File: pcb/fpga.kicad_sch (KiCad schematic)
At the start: 60 parts, among them J1 DE15_Socket_HighDensity, U1 XC7A50T-FTG256, U2 410-251-B, U3 S70KL1283DPBHV020, U4 W25Q128JVS, Y1 ASE-20MHz

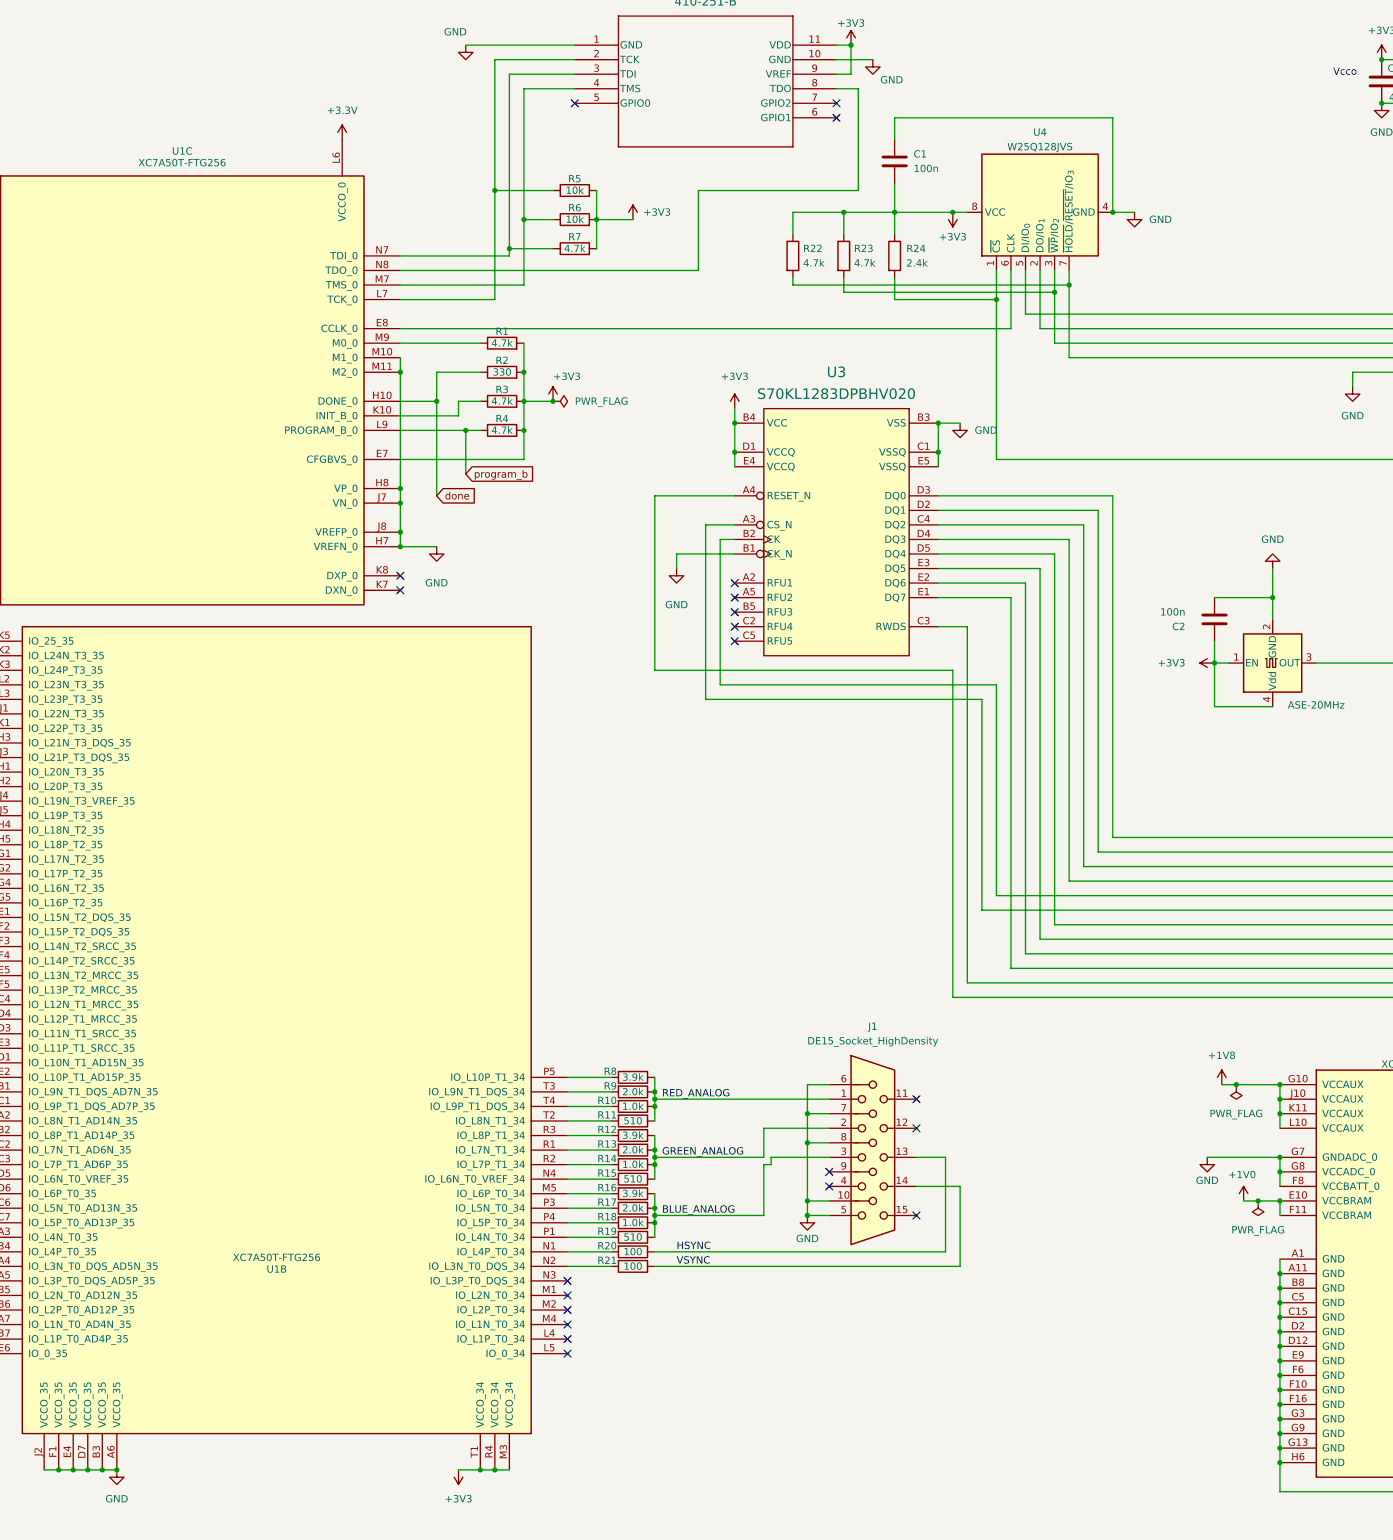
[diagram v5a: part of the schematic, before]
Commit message: pcb: address feedback
- make rgb565 resistor ladder
- add 1v0 diode
- clean up pwr flags
- remove unused mcu-sd spi
- use labels in mcu
- fix broken rgb diode
- connect usblc pin 5 to vbus
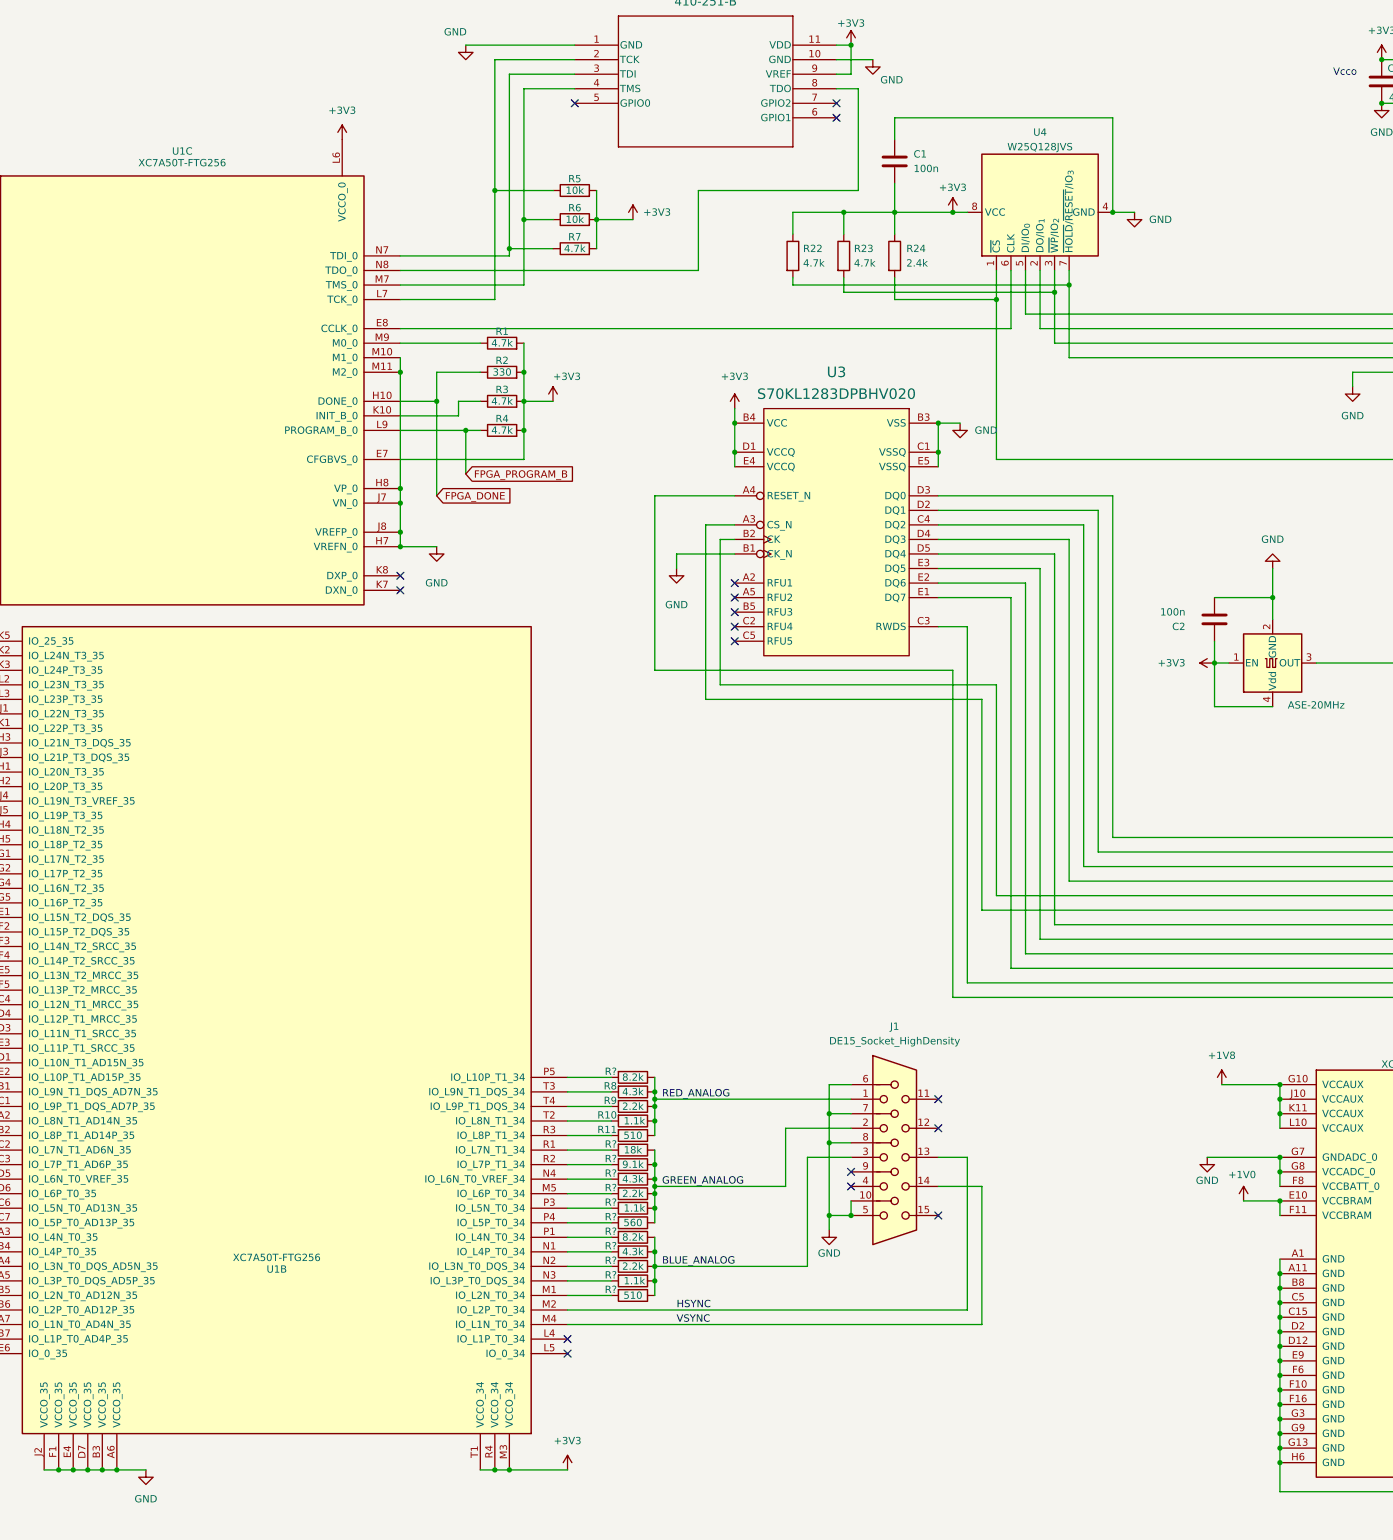
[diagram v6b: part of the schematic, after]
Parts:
- removed R12, R16: 3.9k, Resistor_SMD:R_0805_2012Metric_Pad1.20x1.40mm_HandSolder, symbol Device:R
- removed R13, R17: 2.0k, Resistor_SMD:R_0805_2012Metric_Pad1.20x1.40mm_HandSolder, symbol Device:R
- removed R14, R18: 1.0k, Resistor_SMD:R_0805_2012Metric_Pad1.20x1.40mm_HandSolder, symbol Device:R
- removed R15, R19: 510, Resistor_SMD:R_0805_2012Metric_Pad1.20x1.40mm_HandSolder, symbol Device:R
- removed R20, R21: 100, Resistor_SMD:R_0805_2012Metric_Pad1.20x1.40mm_HandSolder, symbol Device:R
- added R? (x2): 1.1k, Resistor_SMD:R_0805_2012Metric_Pad1.20x1.40mm_HandSolder, symbol Device:R
- added R?: 510, Resistor_SMD:R_0805_2012Metric_Pad1.20x1.40mm_HandSolder, symbol Device:R
- added R?: 560, Resistor_SMD:R_0805_2012Metric_Pad1.20x1.40mm_HandSolder, symbol Device:R
- added R? (x2): 2.2k, Resistor_SMD:R_0805_2012Metric_Pad1.20x1.40mm_HandSolder, symbol Device:R
- added R? (x2): 8.2k, Resistor_SMD:R_0805_2012Metric_Pad1.20x1.40mm_HandSolder, symbol Device:R
- added R?: 9.1k, Resistor_SMD:R_0805_2012Metric_Pad1.20x1.40mm_HandSolder, symbol Device:R
- added R? (x2): 4.3k, Resistor_SMD:R_0805_2012Metric_Pad1.20x1.40mm_HandSolder, symbol Device:R
- added R?: 18k, Resistor_SMD:R_0805_2012Metric_Pad1.20x1.40mm_HandSolder, symbol Device:R
- R10: value 1.0k -> 1.1k
- R8: value 3.9k -> 4.3k
- R9: value 2.0k -> 2.2k
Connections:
- net +3.3V is gone; now on net +3V3: U1.L6 (VCCO_0)
- net BLUE_ANALOG: now also R?.1, R?.1, R?.1, R?.1, R?.1
- net GREEN_ANALOG: now also R?.1, R?.1, R?.1, R?.1, R?.1, R?.1
- net HSYNC: now also U1.M2 (IO_L2P_T0_34)
- net RED_ANALOG: now also R?.1
- net VSYNC: now also U1.M4 (IO_L1N_T0_34)
- net at U1.N4 (IO_L6N_T0_VREF_34): now also R?.2
- net at U1.R1 (IO_L7N_T1_34): now also R?.2
- net at R11.2: now also U1.R3 (IO_L8P_T1_34); no longer U1.T2 (IO_L8N_T1_34)
- net at U1.M1 (IO_L2N_T0_34): now also R?.2
- net at U1.M5 (IO_L6P_T0_34): now also R?.2
- net at U1.N1 (IO_L4P_T0_34): now also R?.2
- net at U1.N2 (IO_L3N_T0_DQS_34): now also R?.2
- net at U1.N3 (IO_L3P_T0_DQS_34): now also R?.2
- net at U1.P1 (IO_L4N_T0_34): now also R?.2
- net at U1.P3 (IO_L5N_T0_34): now also R?.2
- net at U1.P4 (IO_L5P_T0_34): now also R?.2
- net at U1.P5 (IO_L10P_T1_34): now also R?.2; no longer R8.2
- net at U1.R2 (IO_L7P_T1_34): now also R?.2
- net at U1.T3 (IO_L9N_T1_DQS_34): now also R8.2; no longer R9.2
- net at R10.2: now also U1.T2 (IO_L8N_T1_34); no longer U1.T4 (IO_L9P_T1_DQS_34)
- net done renamed FPGA_DONE
- net program_b renamed FPGA_PROGRAM_B
- new net: R9.2, U1.T4 (IO_L9P_T1_DQS_34)
- no-connect marks 129 -> 125
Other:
- moved on the sheet: J1, R10, R11, R8, R9

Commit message: pcb
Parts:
- removed R5, R6: 10k, Resistor_SMD:R_0805_2012Metric_Pad1.20x1.40mm_HandSolder, symbol Device:R
- removed R7: 4.7k, Resistor_SMD:R_0805_2012Metric_Pad1.20x1.40mm_HandSolder, symbol Device:R
- removed U2: 410-251-B, 410_251_B:IC11_410-251-B_DGT, symbol 410-251-B:410-251-B
- added D1, D2: blue?, LED_SMD:LED_0805_2012Metric_Pad1.15x1.40mm_HandSolder, symbol Device:LED
- added D3: LED_ARGB, LED_ARGB:SON4_APTF1616LSEEZGKQBKC_KNB, symbol APTF1616LSEEZGKQBKC:APTF1616LSEEZGKQBKC
- added J1: FPGA_DEBUG, Connector_PinHeader_2.54mm:PinHeader_2x07_P2.54mm_Vertical, symbol Connector_Generic:Conn_02x07_Odd_Even
- added R1, R2: 10k, Resistor_SMD:R_0805_2012Metric_Pad1.20x1.40mm_HandSolder, symbol Device:R
- added R23, R24: 1k, Resistor_SMD:R_0805_2012Metric_Pad1.20x1.40mm_HandSolder, symbol Device:R
- added R28: 51, Resistor_SMD:R_0805_2012Metric_Pad1.20x1.40mm_HandSolder, symbol Device:R
- added R29, R30: 22, Resistor_SMD:R_0805_2012Metric_Pad1.20x1.40mm_HandSolder, symbol Device:R
- gave numbers to parts that had none: 12
- renumbered J1 to J2, R22 to R25, R23 to R26, R24 to R27, R1 to R3, R2 to R4, R3 to R5, R4 to R6, U3 to U2, U4 to U3
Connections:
- net +3V3: now also D3.1, J1.2 (Pin_2), R1.1, R2.1
- net FPGA_DONE: now also R24.1
- net FPGA_PROGRAM_B: now also R23.1
- net GND: now also D1.1 (K), D2.1 (K), J1.1 (Pin_1), J1.11 (Pin_11), J1.13 (Pin_13), J1.3 (Pin_3), J1.5 (Pin_5), J1.7 (Pin_7), J1.9 (Pin_9)
- net TCK_0: now reaches U1.M7 (TMS_0)
- net TCK_0: now also J1.6 (Pin_6), R2.2
- net TDI_0: now reaches U1.N7 (TDI_0)
- net TDI_0: now also J1.10 (Pin_10)
- net TMS_0: now reaches U1.L7 (TCK_0)
- net TMS_0: now also J1.4 (Pin_4), R1.2
- net TDO_0: now reaches U1.N8 (TDO_0)
- net TDO_0: now also J1.8 (Pin_8)
- net at U1.A8 (IO_L2P_T0_AD8P_15): now also R28.2
- net at U1.A9 (IO_L2N_T0_AD8N_15): now also R29.2
- net at U1.B9 (IO_L3P_T0_DQS_AD1P_15): now also R30.2
- new net: D2.2 (A), R24.2
- new net: D3.2, R28.1
- new net: D3.3, R29.1
- new net: D3.4, R30.1
- new net: D1.2 (A), R23.2
- no-connect marks 125 -> 121

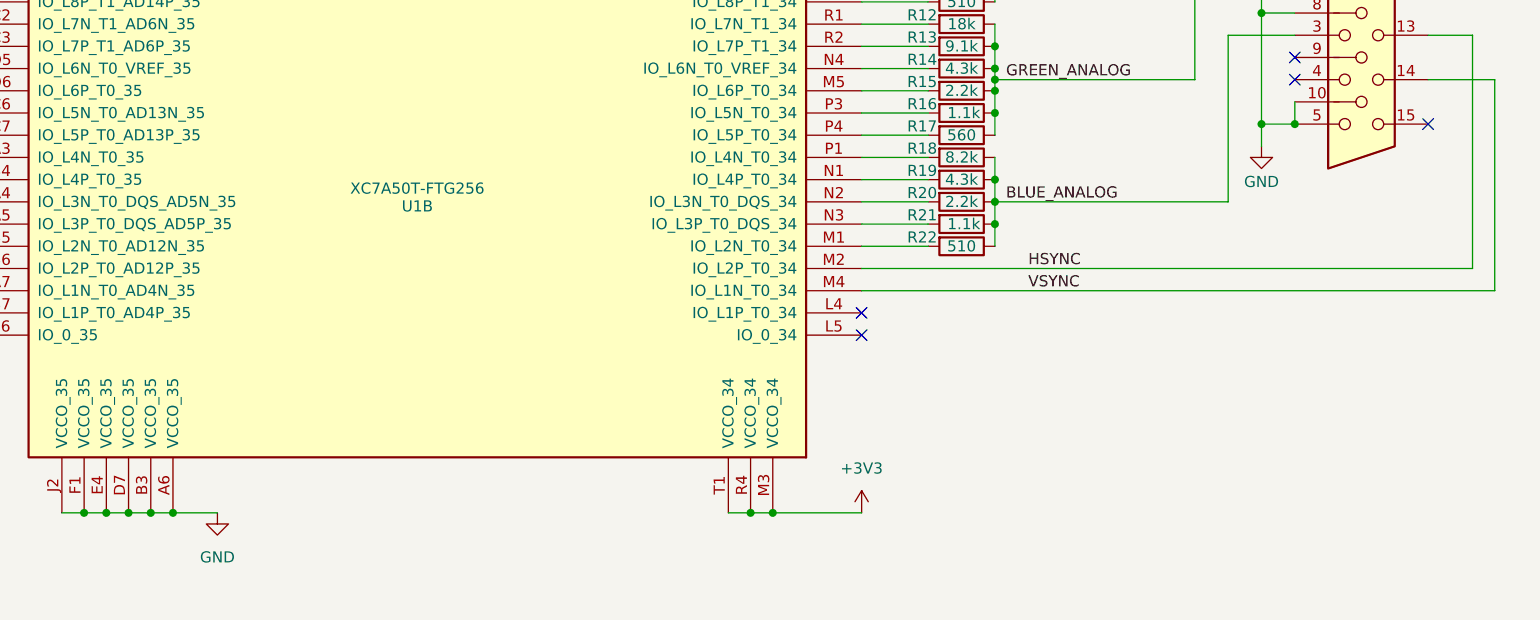
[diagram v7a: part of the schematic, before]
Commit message: new VGA model and footprint added
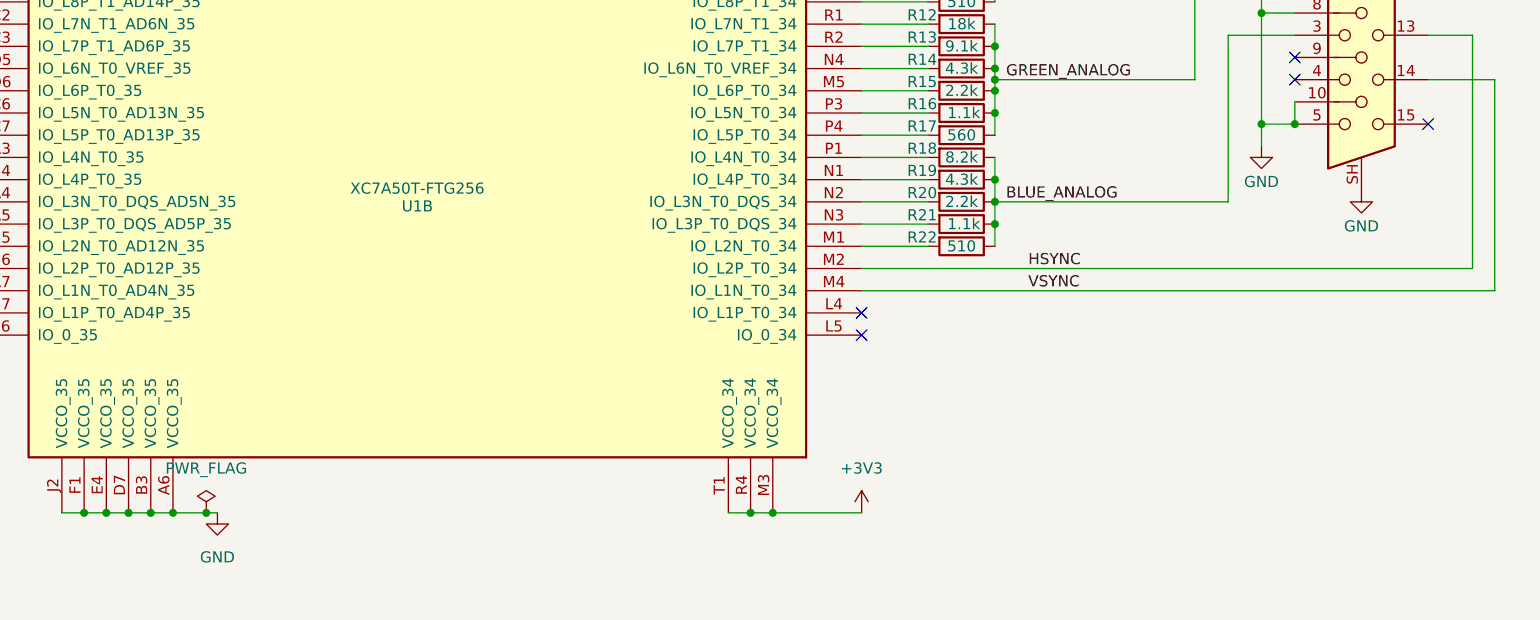
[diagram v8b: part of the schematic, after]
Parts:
- J2: footprint Connector_Dsub:DSUB-15_Socket_EdgeMount_P2.77mm -> L77HDE15SD1CH4FVGA:AMPHENOL_L77HDE15SD1CH4FVGA; symbol Connector:DE15_Socket_HighDensity -> Connector:DE15_Socket_HighDensity_MountingHoles
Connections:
- net GND: now also J2.SH
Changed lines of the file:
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@@
 	)
 	(junction
+		(at 43.18 274.32)
+		(diameter 0)
+		(color 0 0 0 0)
+	)
+	(junction
 		(at 360.68 27.94)
 		(diameter 0)
@@
 	(wire
 		(pts
+			(xy 43.18 274.32) (xy 39.37 274.32)
+		)
+		(stroke
+			(width 0)
+			(type default)
+		)
+	)
+	(wire
+		(pts
 			(xy 118.11 246.38) (xy 187.96 246.38)
 		)
@@
 	(wire
 		(pts
-			(xy 44.45 274.32) (xy 39.37 274.32)
+			(xy 44.45 274.32) (xy 43.18 274.32)
 		)
 		(stroke
@@
 	)
 	(symbol
-		(lib_id "Connector:DE15_Socket_HighDensity")
+		(lib_id "Connector:DE15_Socket_HighDensity_MountingHoles")
 		(at 175.26 219.71 0)
 		(unit 1)
@@
 			)
 		)
-		(property "Footprint" "Connector_Dsub:DSUB-15_Socket_EdgeMount_P2.77mm"
+		(property "Footprint" "L77HDE15SD1CH4FVGA:AMPHENOL_L77HDE15SD1CH4FVGA"
 			(at 151.13 209.55 0)
 			(hide yes)
@@
 			)
 		)
-		(property "Description" "15-pin D-SUB connector, socket (female), High density (3 columns), Triple Row, Generic, VGA-connector"
+		(property "Description" "15-pin D-SUB connector, socket (female), High density (3 columns), Triple Row, Generic, VGA-connector, Mounting Hole"
 			(at 175.26 219.71 0)
 			(hide yes)
@@
 		(pin "7"
 		)
+		(pin "SH"
+		)
 		(instances
 			(project "tdt4295"
@@
 	)
 	(symbol
+		(lib_id "power:GND")
+		(at 175.26 237.49 0)
+		(unit 1)
+		(body_style 1)
+		(exclude_from_sim no)
+		(in_bom yes)
+		(on_board yes)
+		(in_pos_files yes)
+		(dnp no)
+		(property "Reference" "#PWR037"
+			(at 175.26 243.84 0)
+			(hide yes)
+			(show_name no)
+			(do_not_autoplace no)
+			(effects
+				(font
+					(size 1.27 1.27)
+				)
+			)
+		)
+		(property "Value" "GND"
+			(at 175.26 241.554 0)
+			(show_name no)
+			(do_not_autoplace no)
+			(effects
+				(font
+					(size 1.27 1.27)
+				)
+			)
+		)
+		(property "Footprint" ""
+			(at 175.26 237.49 0)
+			(hide yes)
+			(show_name no)
+			(do_not_autoplace no)
+			(effects
+				(font
+					(size 1.27 1.27)
+				)
+			)
+		)
+		(property "Datasheet" ""
+			(at 175.26 237.49 0)
+			(hide yes)
+			(show_name no)
+			(do_not_autoplace no)
+			(effects
+				(font
+					(size 1.27 1.27)
+				)
+			)
+		)
+		(property "Description" "Power symbol creates a global label with name \"GND\" , ground"
+			(at 175.26 237.49 0)
+			(hide yes)
+			(show_name no)
+			(do_not_autoplace no)
+			(effects
+				(font
+					(size 1.27 1.27)
+				)
+			)
+		)
+		(pin "1"
+		)
+		(instances
+			(project "tdt4295"
+				(path "/603dd496-f9c4-4a31-9104-19eec41ebc98/55913984-0b9b-45b1-b632-d56e73135cfc"
+					(reference "#PWR037")
+					(unit 1)
+				)
+			)
+		)
+	)
+	(symbol
 		(lib_id "power:+3V3")
 		(at 387.35 41.91 0)
@@
 					(unit 1)
 				)
+			)
+		)
+	)
+	(symbol
+		(lib_id "power:PWR_FLAG")
+		(at 43.18 274.32 0)
+		(unit 1)
+		(body_style 1)
+		(exclude_from_sim no)
+		(in_bom yes)
+		(on_board yes)
+		(in_pos_files yes)
+		(dnp no)
+		(fields_autoplaced yes)
+		(property "Reference" "#FLG08"
+			(at 43.18 272.415 0)
+			(hide yes)
+			(show_name no)
+			(do_not_autoplace no)
+			(effects
+				(font
+					(size 1.27 1.27)
+				)
+			)
+		)
+		(property "Value" "PWR_FLAG"
+			(at 43.18 269.24 0)
+			(show_name no)
+			(do_not_autoplace no)
+			(effects
+				(font
+					(size 1.27 1.27)
+				)
+			)
+		)
+		(property "Footprint" "Package_DFN_QFN:QFN-16-1EP_4x4mm_P0.65mm_EP2.1x2.1mm"
+			(at 43.18 274.32 0)
+			(hide yes)
+			(show_name no)
+			(do_not_autoplace no)
+			(effects
+				(font
+					(size 1.27 1.27)
+				)
+			)
+		)
+		(property "Datasheet" ""
+			(at 43.18 274.32 0)
+			(hide yes)
+			(show_name no)
+			(do_not_autoplace no)
+			(effects
+				(font
+					(size 1.27 1.27)
+				)
+			)
+		)
+		(property "Description" "Special symbol for telling ERC where power comes from"
+			(at 43.18 274.32 0)
+			(hide yes)
+			(show_name no)
+			(do_not_autoplace no)
+			(effects
+				(font
+					(size 1.27 1.27)
+				)
+			)
+		)
+		(pin "1"
+		)
+		(instances
+			(project "tdt4295"
+				(path "/603dd496-f9c4-4a31-9104-19eec41ebc98/55913984-0b9b-45b1-b632-d56e73135cfc"
+					(reference "#FLG08")
+					(unit 1)
+				)
